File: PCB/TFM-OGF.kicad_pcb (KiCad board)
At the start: 2 copper layers, 74 x 74 mm, 24 parts, among them J1 Alimentación, J10 5V Output, J11 3.3V Output, J2 CAN_Externo, J3 Jumper CAN, J4 Jumper CAN, J5 Lado izquierdo, J6 Lado derecho, J7 Lado izquierdo, J8 Lado derecho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

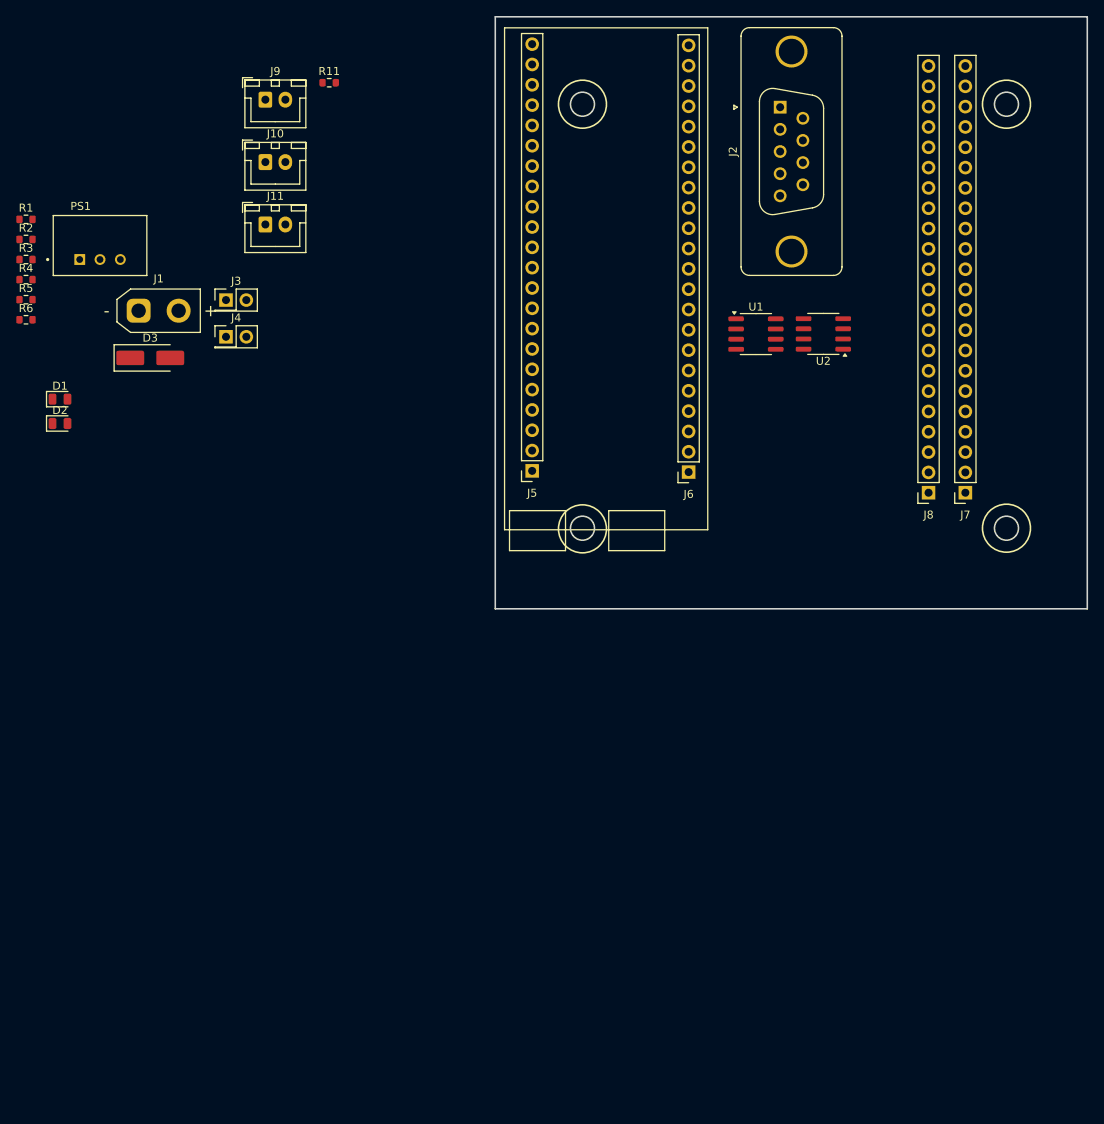
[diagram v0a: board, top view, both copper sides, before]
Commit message: Primera versión de colocar los componentes
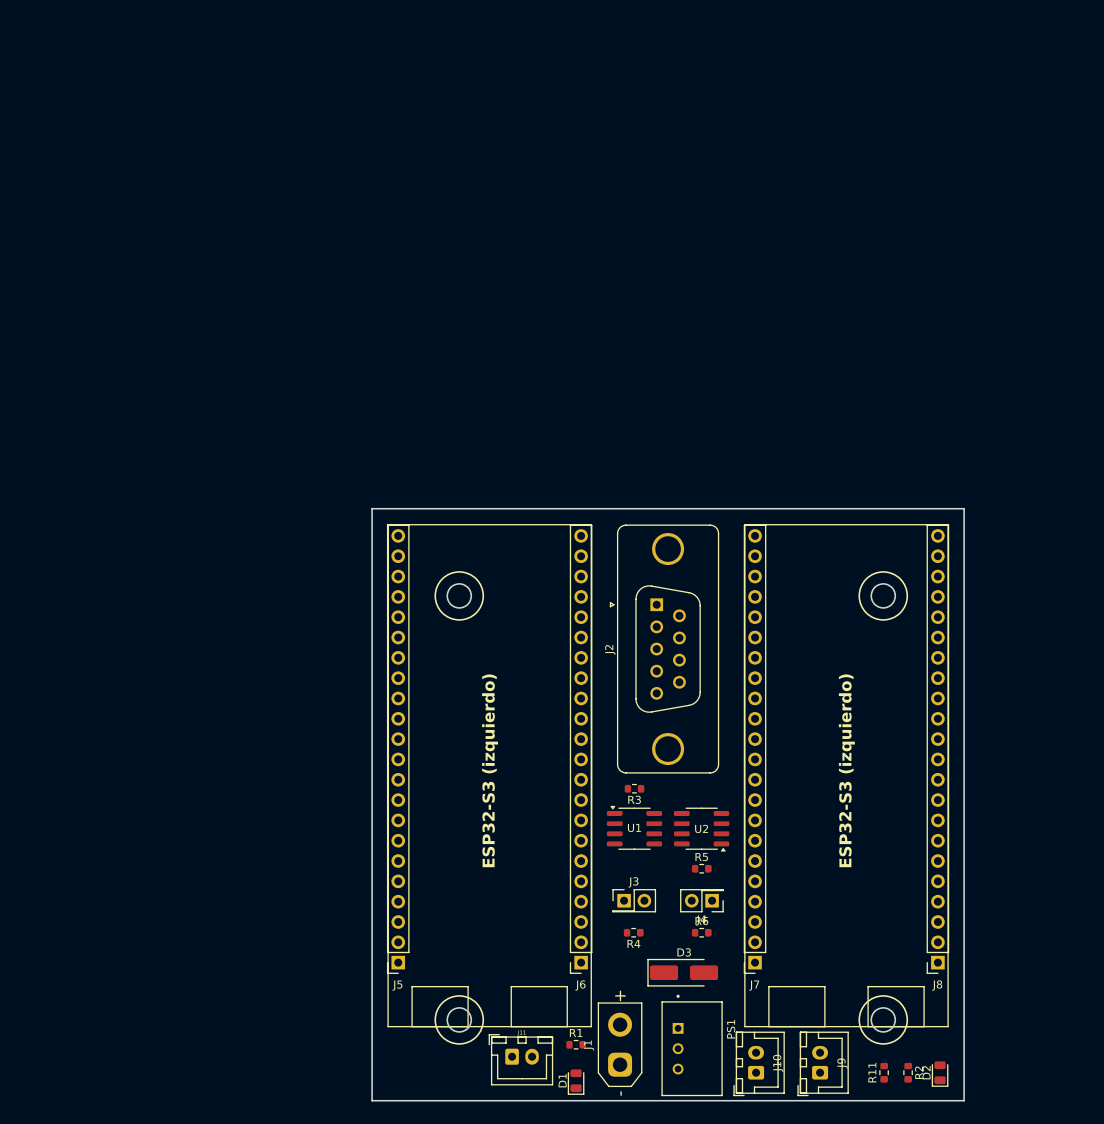
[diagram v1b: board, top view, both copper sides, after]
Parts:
- J9: value Led_Power_Externo -> Led_Pow_Ext
- moved R2 151.7 mm to (167.0, 170.5), turned to -90 degrees
- moved R11 141.9 mm to (164.0, 170.5), turned to 90 degrees
- moved J9 140.0 mm to (156.0, 170.5), turned to 90 degrees
- moved D2 136.7 mm to (171.0, 170.5), turned to 90 degrees
- moved J10 129.3 mm to (148.0, 170.5), turned to 90 degrees
- moved PS1 124.7 mm to (140.0, 167.5), turned to -90 degrees
- moved R1 124.0 mm to (125.5, 167.0)
- moved R6 114.0 mm to (141.2, 153.0)
- moved J1 111.8 mm to (131.0, 169.5), turned to 90 degrees
- moved R4 111.5 mm to (132.7, 153.0), turned to 180 degrees
- moved R5 110.4 mm to (141.2, 145.0)
- moved J11 108.5 mm to (117.5, 168.5)
- moved D1 106.9 mm to (125.5, 171.5), turned to 90 degrees
- moved D3 101.8 mm to (139.0, 158.0)
- moved R3 100.8 mm to (132.8, 135.0), turned to 180 degrees
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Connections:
- J11 pad 2: 3.3V -> 3.3V_1
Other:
- board text added: "ESP32-S3 (izquierdo)"

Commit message: Corrijo orientación de algunas resistencias
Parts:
- turned R2 to 90 degrees
- turned R3 to 0 degrees
- turned R4 to 0 degrees
- renumbered R11 to R7
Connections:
- R2 pad 1: Net-(D2-A) -> 5V
- R2 pad 2: 5V -> Net-(D2-A)
- R3 pad 1: Net-(U1-Rs) -> GND
- R3 pad 2: GND -> Net-(U1-Rs)
- R4 pad 1: CAN_High -> Net-(J3-Pin_1)
- R4 pad 2: Net-(J3-Pin_1) -> CAN_High
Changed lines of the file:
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@@
 	(footprint "Resistor_SMD:R_0603_1608Metric"
 		(layer "F.Cu")
-		(at 167 170.5 -90)
+		(at 167 170.5 90)
 		(descr "Resistor SMD 0603 (1608 Metric), square (rectangular) end terminal, IPC-7351 nominal, (Body size source: IPC-SM-782 page 72, https://www.pcb-3d.com/wordpress/wp-content/uploads/ipc-sm-782a_amendment_1_and_2.pdf), generated with kicad-footprint-generator")
 		(tags "resistor")
@@
 		(attr smd)
 		(fp_line
-			(start -0.237258 0.5225)
-			(end 0.237258 0.5225)
+			(start -0.237258 -0.5225)
+			(end 0.237258 -0.5225)
 			(stroke
 				(width 0.12)
@@
 		)
 		(fp_line
-			(start -0.237258 -0.5225)
-			(end 0.237258 -0.5225)
+			(start -0.237258 0.5225)
+			(end 0.237258 0.5225)
 			(stroke
 				(width 0.12)
@@
 		)
 		(fp_line
-			(start -1.48 0.73)
-			(end -1.48 -0.73)
+			(start 1.48 -0.73)
+			(end 1.48 0.73)
 			(stroke
 				(width 0.05)
@@
 		)
 		(fp_line
-			(start 1.48 0.73)
-			(end -1.48 0.73)
+			(start -1.48 -0.73)
+			(end 1.48 -0.73)
 			(stroke
 				(width 0.05)
@@
 		)
 		(fp_line
-			(start -1.48 -0.73)
-			(end 1.48 -0.73)
+			(start 1.48 0.73)
+			(end -1.48 0.73)
 			(stroke
 				(width 0.05)
@@
 		)
 		(fp_line
-			(start 1.48 -0.73)
-			(end 1.48 0.73)
+			(start -1.48 0.73)
+			(end -1.48 -0.73)
 			(stroke
 				(width 0.05)
@@
 		)
 		(fp_line
-			(start -0.8 0.4125)
-			(end -0.8 -0.4125)
+			(start 0.8 -0.4125)
+			(end 0.8 0.4125)
 			(stroke
 				(width 0.1)
@@
 		)
 		(fp_line
-			(start 0.8 0.4125)
-			(end -0.8 0.4125)
+			(start -0.8 -0.4125)
+			(end 0.8 -0.4125)
 			(stroke
 				(width 0.1)
@@
 		)
 		(fp_line
-			(start -0.8 -0.4125)
-			(end 0.8 -0.4125)
+			(start 0.8 0.4125)
+			(end -0.8 0.4125)
 			(stroke
 				(width 0.1)
@@
 		)
 		(fp_line
-			(start 0.8 -0.4125)
-			(end 0.8 0.4125)
+			(start -0.8 0.4125)
+			(end -0.8 -0.4125)
 			(stroke
 				(width 0.1)
@@
 		)
 		(pad "1" smd roundrect
-			(at -0.825 0 270)
+			(at -0.825 0 90)
 			(size 0.8 0.95)
 			(layers "F.Cu" "F.Mask" "F.Paste")
 			(roundrect_rratio 0.25)
-			(net 3 "Net-(D2-A)")
+			(net 4 "5V")
 			(pintype "passive")
 		)
 		(pad "2" smd roundrect
-			(at 0.825 0 270)
+			(at 0.825 0 90)
 			(size 0.8 0.95)
 			(layers "F.Cu" "F.Mask" "F.Paste")
 			(roundrect_rratio 0.25)
-			(net 4 "5V")
+			(net 3 "Net-(D2-A)")
 			(pintype "passive")
 		)
@@
 	(footprint "Resistor_SMD:R_0603_1608Metric"
 		(layer "F.Cu")
-		(at 132.7 153 180)
+		(at 132.7 153)
 		(descr "Resistor SMD 0603 (1608 Metric), square (rectangular) end terminal, IPC-7351 nominal, (Body size source: IPC-SM-782 page 72, https://www.pcb-3d.com/wordpress/wp-content/uploads/ipc-sm-782a_amendment_1_and_2.pdf), generated with kicad-footprint-generator")
 		(tags "resistor")
@@
 		(attr smd)
 		(fp_line
-			(start -0.237258 0.5225)
-			(end 0.237258 0.5225)
+			(start -0.237258 -0.5225)
+			(end 0.237258 -0.5225)
 			(stroke
 				(width 0.12)
@@
 		)
 		(fp_line
-			(start -0.237258 -0.5225)
-			(end 0.237258 -0.5225)
+			(start -0.237258 0.5225)
+			(end 0.237258 0.5225)
 			(stroke
 				(width 0.12)
@@
 		)
 		(fp_line
-			(start 1.48 0.73)
-			(end -1.48 0.73)
+			(start -1.48 -0.73)
+			(end 1.48 -0.73)
 			(stroke
 				(width 0.05)
@@
 		)
 		(fp_line
-			(start 1.48 -0.73)
-			(end 1.48 0.73)
+			(start -1.48 0.73)
+			(end -1.48 -0.73)
 			(stroke
 				(width 0.05)
@@
 		)
 		(fp_line
-			(start -1.48 0.73)
-			(end -1.48 -0.73)
+			(start 1.48 -0.73)
+			(end 1.48 0.73)
 			(stroke
 				(width 0.05)
@@
 		)
 		(fp_line
-			(start -1.48 -0.73)
-			(end 1.48 -0.73)
+			(start 1.48 0.73)
+			(end -1.48 0.73)
 			(stroke
 				(width 0.05)
@@
 		)
 		(fp_line
-			(start 0.8 0.4125)
-			(end -0.8 0.4125)
+			(start -0.8 -0.4125)
+			(end 0.8 -0.4125)
 			(stroke
 				(width 0.1)
@@
 		)
 		(fp_line
-			(start 0.8 -0.4125)
-			(end 0.8 0.4125)
+			(start -0.8 0.4125)
+			(end -0.8 -0.4125)
 			(stroke
 				(width 0.1)
@@
 		)
 		(fp_line
-			(start -0.8 0.4125)
-			(end -0.8 -0.4125)
+			(start 0.8 -0.4125)
+			(end 0.8 0.4125)
 			(stroke
 				(width 0.1)
@@
 		)
 		(fp_line
-			(start -0.8 -0.4125)
-			(end 0.8 -0.4125)
+			(start 0.8 0.4125)
+			(end -0.8 0.4125)
 			(stroke
 				(width 0.1)
@@
 		)
 		(pad "1" smd roundrect
-			(at -0.825 0 180)
+			(at -0.825 0)
 			(size 0.8 0.95)
 			(layers "F.Cu" "F.Mask" "F.Paste")
 			(roundrect_rratio 0.25)
-			(net 8 "CAN_High")
+			(net 14 "Net-(J3-Pin_1)")
 			(pintype "passive")
 		)
 		(pad "2" smd roundrect
-			(at 0.825 0 180)
+			(at 0.825 0)
 			(size 0.8 0.95)
 			(layers "F.Cu" "F.Mask" "F.Paste")
 			(roundrect_rratio 0.25)
-			(net 14 "Net-(J3-Pin_1)")
+			(net 8 "CAN_High")
 			(pintype "passive")
 		)
@@
 	(footprint "Resistor_SMD:R_0603_1608Metric"
 		(layer "F.Cu")
-		(at 132.8 135 180)
+		(at 132.8 135)
 		(descr "Resistor SMD 0603 (1608 Metric), square (rectangular) end terminal, IPC-7351 nominal, (Body size source: IPC-SM-782 page 72, https://www.pcb-3d.com/wordpress/wp-content/uploads/ipc-sm-782a_amendment_1_and_2.pdf), generated with kicad-footprint-generator")
 		(tags "resistor")
@@
 		(attr smd)
 		(fp_line
-			(start -0.237258 0.5225)
-			(end 0.237258 0.5225)
+			(start -0.237258 -0.5225)
+			(end 0.237258 -0.5225)
 			(stroke
 				(width 0.12)
@@
 		)
 		(fp_line
-			(start -0.237258 -0.5225)
-			(end 0.237258 -0.5225)
+			(start -0.237258 0.5225)
+			(end 0.237258 0.5225)
 			(stroke
 				(width 0.12)
@@
 		)
 		(fp_line
-			(start 1.48 0.73)
-			(end -1.48 0.73)
+			(start -1.48 -0.73)
+			(end 1.48 -0.73)
 			(stroke
 				(width 0.05)
@@
 		)
 		(fp_line
-			(start 1.48 -0.73)
-			(end 1.48 0.73)
+			(start -1.48 0.73)
+			(end -1.48 -0.73)
 			(stroke
 				(width 0.05)
@@
 		)
 		(fp_line
-			(start -1.48 0.73)
-			(end -1.48 -0.73)
+			(start 1.48 -0.73)
+			(end 1.48 0.73)
 			(stroke
 				(width 0.05)
@@
 		)
 		(fp_line
-			(start -1.48 -0.73)
-			(end 1.48 -0.73)
+			(start 1.48 0.73)
+			(end -1.48 0.73)
 			(stroke
 				(width 0.05)
@@
 		)
 		(fp_line
-			(start 0.8 0.4125)
-			(end -0.8 0.4125)
+			(start -0.8 -0.4125)
+			(end 0.8 -0.4125)
 			(stroke
 				(width 0.1)
@@
 		)
 		(fp_line
-			(start 0.8 -0.4125)
-			(end 0.8 0.4125)
+			(start -0.8 0.4125)
+			(end -0.8 -0.4125)
 			(stroke
 				(width 0.1)
@@
 		)
 		(fp_line
-			(start -0.8 0.4125)
-			(end -0.8 -0.4125)
+			(start 0.8 -0.4125)
+			(end 0.8 0.4125)
 			(stroke
 				(width 0.1)
@@
 		)
 		(fp_line
-			(start -0.8 -0.4125)
-			(end 0.8 -0.4125)
+			(start 0.8 0.4125)
+			(end -0.8 0.4125)
 			(stroke
 				(width 0.1)
@@
 		)
 		(pad "1" smd roundrect
-			(at -0.825 0 180)
+			(at -0.825 0)
 			(size 0.8 0.95)
 			(layers "F.Cu" "F.Mask" "F.Paste")
 			(roundrect_rratio 0.25)
-			(net 19 "Net-(U1-Rs)")
+			(net 1 "GND")
 			(pintype "passive")
 		)
 		(pad "2" smd roundrect
-			(at 0.825 0 180)
+			(at 0.825 0)
 			(size 0.8 0.95)
 			(layers "F.Cu" "F.Mask" "F.Paste")
 			(roundrect_rratio 0.25)
-			(net 1 "GND")
+			(net 19 "Net-(U1-Rs)")
 			(pintype "passive")
 		)
@@
 		(descr "Resistor SMD 0603 (1608 Metric), square (rectangular) end terminal, IPC-7351 nominal, (Body size source: IPC-SM-782 page 72, https://www.pcb-3d.com/wordpress/wp-content/uploads/ipc-sm-782a_amendment_1_and_2.pdf), generated with kicad-footprint-generator")
 		(tags "resistor")
-		(property "Reference" "R11"
+		(property "Reference" "R7"
 			(at 0 -1.43 90)
 			(layer "F.SilkS")

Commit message: Completo placa
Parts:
- added G1: LOGO, LOGO, B.Cu at (135.0, 146.0)
- added G2: LOGO, LOGO, F.Cu at (103.5, 169.5)
- added G3: LOGO, LOGO, B.Cu at (137.0, 113.0)
- moved R5 0.50 mm to (141.2, 144.5)
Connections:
- J7 pad 8: TxCANDer_G10_2 -> RxCANDer_G09_2
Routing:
- net GND: track 0.00 -> 196.8 mm, vias 0 -> 1
- net 5V: track 0.00 -> 100.7 mm
- net 3.3V_1: track 0.00 -> 85.1 mm
- net CAN_Low: track 0.00 -> 52.2 mm, vias 0 -> 1
- net CAN_High: track 0.00 -> 49.6 mm, vias 0 -> 2
- net 3.3V_2: track 0.00 -> 39.7 mm, vias 0 -> 1
- net Vin: track 0.00 -> 21.9 mm
- net Net-(J9-Pin_2): track 0.00 -> 8.69 mm
- net TxCANIzq_G45_1: track 0.00 -> 4.55 mm
- net RxCANDer_G09_2: track 0.00 -> 4.55 mm
- net TxCANDer_G10_2: track 0.00 -> 4.36 mm
- net RxCANIzq_G48_1: track 0.00 -> 4.36 mm
- net Net-(J4-Pin_1): track 0.00 -> 4.20 mm
- net Net-(J3-Pin_1): track 0.00 -> 4.16 mm
- net Net-(D2-A): track 0.00 -> 4.05 mm
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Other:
- board text added: "GND 5V G14 G13 G12 G11 G10 G09 G46 G03 G08 G18 G17 G16 G15 G07 G06 G05 G04 RST 3V3 3V3"
- board text added: "GND GND G19 G20 G21 G47 G48 G45 G00 G35 G36 G37 G38 G39 G40 G41 G42 G02 G01 RX TX GND"
- board text added: "SLP OGF 2025"
